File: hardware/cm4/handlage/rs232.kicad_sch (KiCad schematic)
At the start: 13 parts, among them J3 D340 PC (4P4C), U3 ADuM5211, U5 MAX3232E

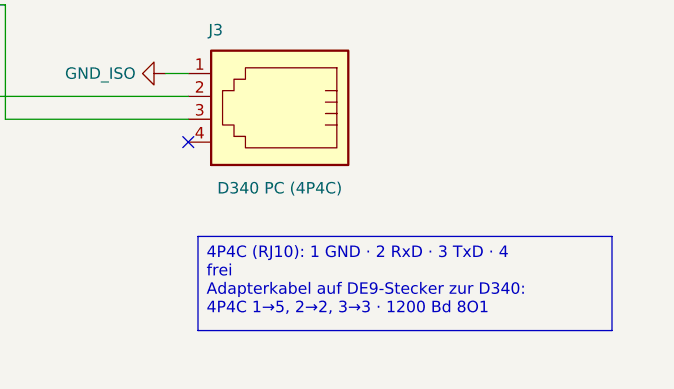
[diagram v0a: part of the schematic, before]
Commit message: CM4-Schaltplan: Handänderungen übernommen (Handlage für 8 Blätter, 2 Texte zurückgeführt); Kastenhöhen aus gemessenen Zeichenbreiten
Co-Authored-By: Claude Opus 5.5 <noreply@anthropic.com>
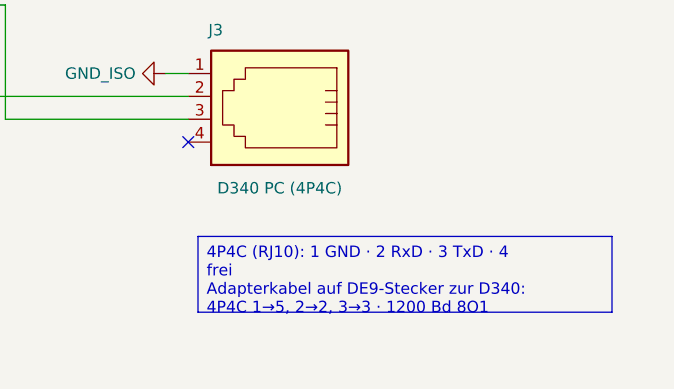
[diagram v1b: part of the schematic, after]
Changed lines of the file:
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@@
 	(text "isolierte Seite (GND_ISO)" (exclude_from_sim no) (at 139.42 174.88 0) (effects (font (size 1.27 1.27) italic) (justify left bottom)))
 	(text "ADuM5211:\nTrenner mit isolierter 3,3-V-Versorgung\n(VSEL = GND_ISO)\ndtoverlay=uart3" (exclude_from_sim no) (at 89.66 167.13 0) (effects (font (size 1.27 1.27) italic) (justify left bottom)))
-	(text_box "4P4C (RJ10): 1 GND · 2 RxD · 3 TxD · 4 frei\nAdapterkabel auf DE9-Stecker zur D340: 4P4C 1→5, 2→2, 3→3 · 1200 Bd 8O1" (exclude_from_sim no) (at 275.4 160.34 0) (size 46 10.46) (margins 0.9525 0.9525 0.9525 0.9525) (stroke (width 0.1) (type solid) (color 132 132 132 1)) (fill (type color) (color 255 255 230 1)) (effects (font (size 1.27 1.27)) (justify left top)))
+	(text_box "4P4C (RJ10): 1 GND · 2 RxD · 3 TxD · 4 frei\nAdapterkabel auf DE9-Stecker zur D340: 4P4C 1→5, 2→2, 3→3 · 1200 Bd 8O1" (exclude_from_sim no) (at 275.4 160.34 0) (size 46 8.42) (margins 0.9525 0.9525 0.9525 0.9525) (stroke (width 0.1) (type solid) (color 132 132 132 1)) (fill (type color) (color 255 255 230 1)) (effects (font (size 1.27 1.27)) (justify left top)))
 	)
